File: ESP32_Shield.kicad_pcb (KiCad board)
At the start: 4 copper layers, 69 x 40.6 mm, 36 parts, among them J1 BME280, SHT40 Module, J10 SCD40 Module, J11 Conn_01x03, J12 Conn_01x03, J2 SCD40 Module, J3 Conn_01x02, J4 Qwiic_Vertical, J5 Conn_01x02, J6 Conn_01x02, J7 Conn_01x03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

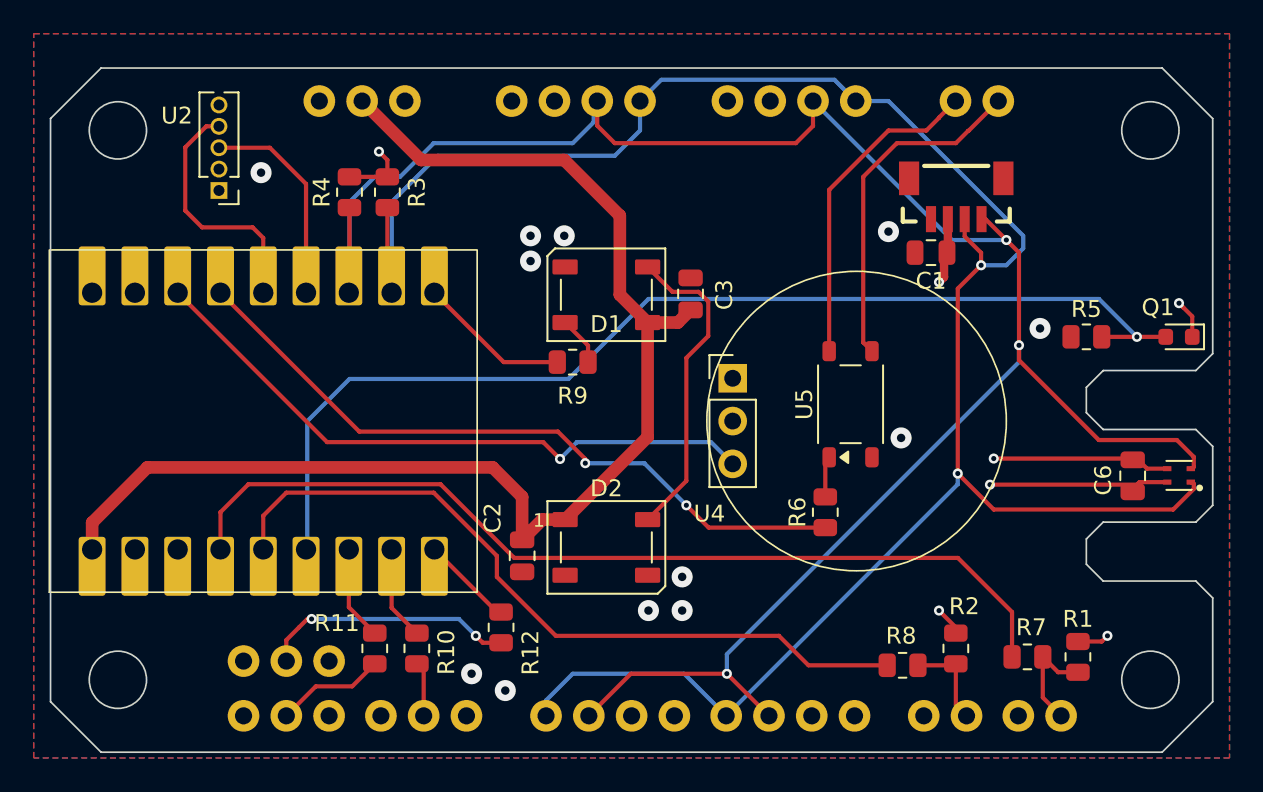
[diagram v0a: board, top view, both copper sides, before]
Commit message: remove fix soldered tempertaure sesor
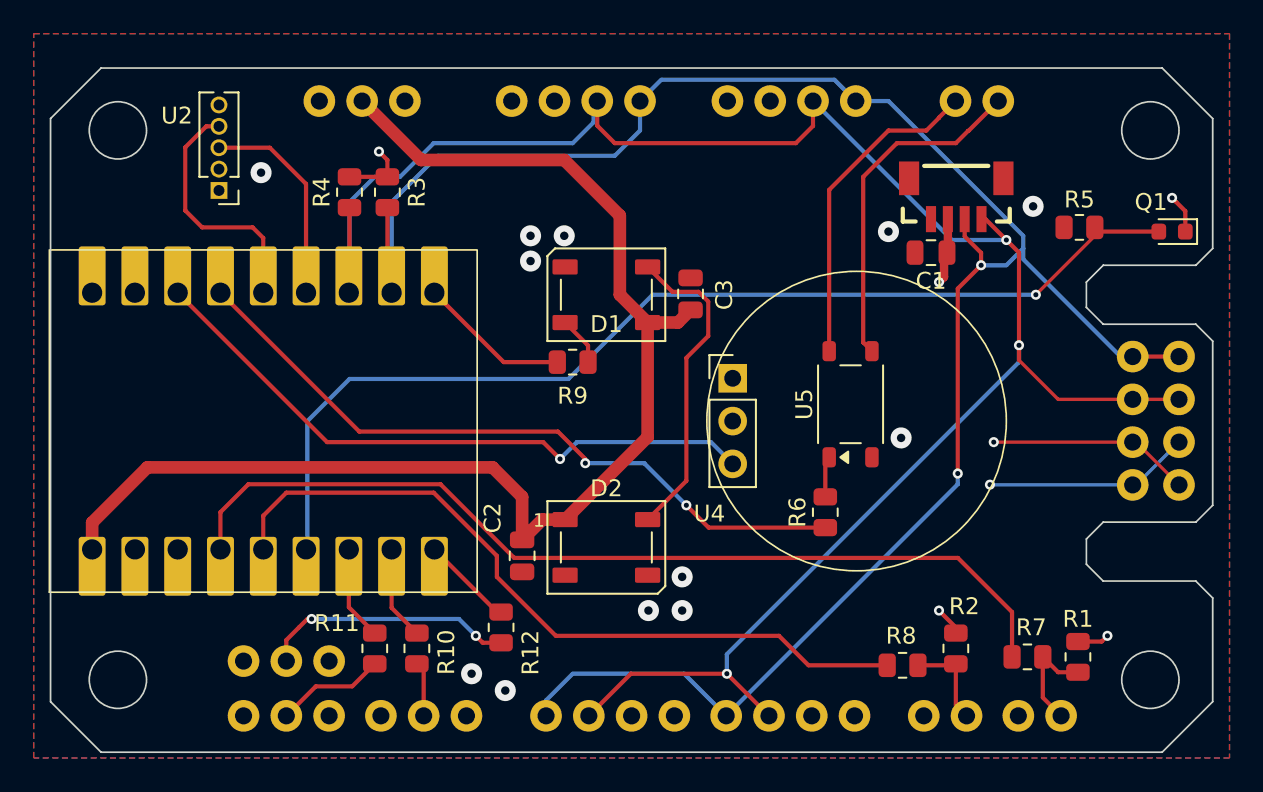
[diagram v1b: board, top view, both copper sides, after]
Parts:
- removed C6: 100n, Capacitor_SMD:C_0805_2012Metric
- removed U3: SHT40, PCM_SparkFun-Sensor:Sensirion_DFN-4_1.5x1.5mm_P0.8mm_SHT4x_NoCentralPad
- added J13: SCD40 Module, PCM_SparkFun-Connector:1x04_P2.54mm, F.Cu at (155.2, 92.3)
- added J14: BME280, SHT40 Module, PCM_SparkFun-Connector:1x04_P2.54mm, F.Cu at (158.0, 92.3)
- moved R5 6.51 mm to (152.1, 77.0)
- moved Q1 6.26 mm to (157.6, 77.2)
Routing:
- net SDA: track 125.1 -> 121.3 mm
- net SCK: track 122.4 -> 119.2 mm
- net GND: track 10.6 -> 12.3 mm
- net +3V3: track 24.4 -> 25.9 mm
- net PhotoMeas: track 64.6 -> 63.3 mm
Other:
- outline, holes or cut-outs redrawn

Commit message: add silk screen and mmWave connector
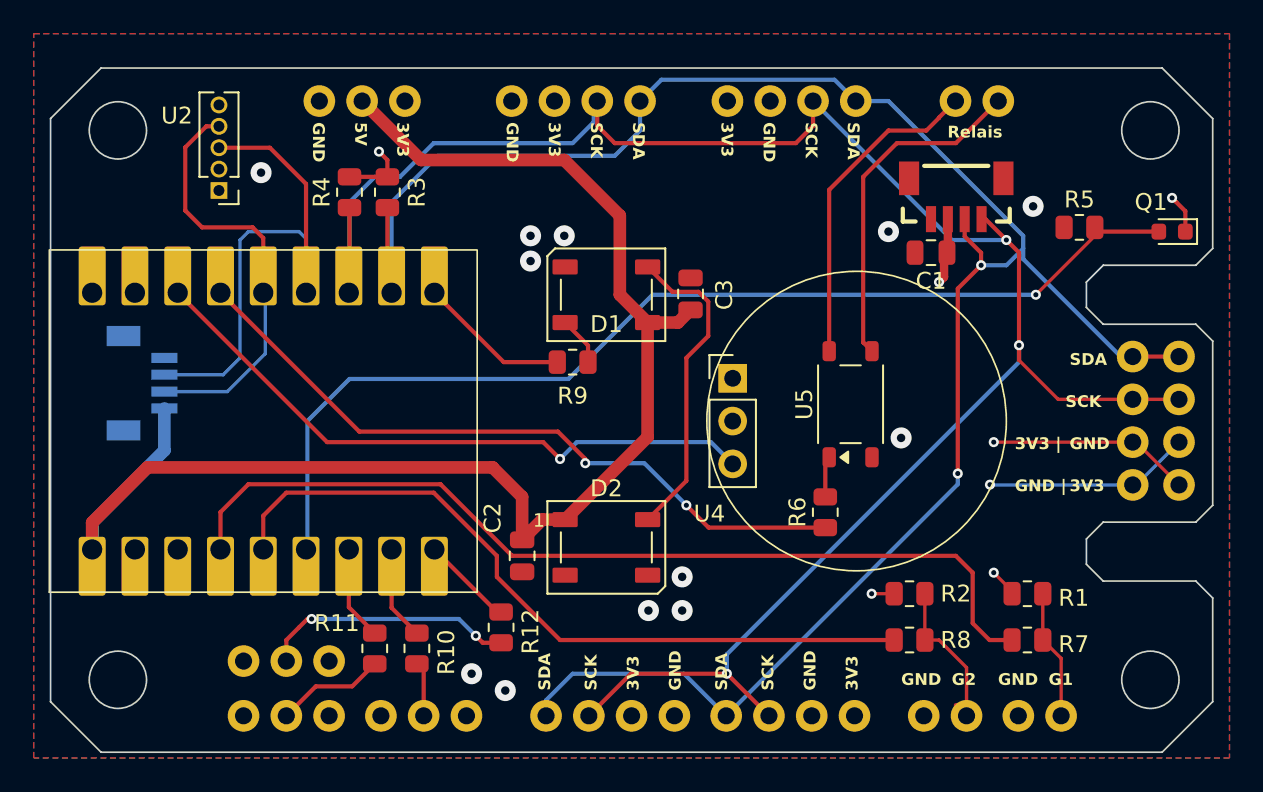
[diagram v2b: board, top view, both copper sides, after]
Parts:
- added J15: mmWave Connector, PCM_SparkFun-Connector:JST_1x04_P1.0mm_Vertical_SMD, B.Cu at (96.2, 86.2)
- moved R1 4.80 mm to (149.0, 98.8), turned to 180 degrees
- moved R2 4.26 mm to (142.0, 98.8), turned to 180 degrees
- moved R8 1.56 mm to (142.0, 101.5)
- moved R7 1.00 mm to (149.0, 101.5)
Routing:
- net UART_RX_mmWAVE: track 12.5 -> 31.9 mm
- net UART_TX_mmWAVE: track 14.8 -> 25.4 mm
- net +5V: track 76.5 -> 86.7 mm
- net Net-(J5-Pin_2): track 5.64 -> 9.66 mm
- net Net-(J6-Pin_2): track 6.42 -> 7.70 mm
- net +3V3: track 25.9 -> 25.3 mm
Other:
- board text added: "3V3"
- board text added: "3V3 |"
- board text added: "5V"
- board text added: "G1"
- board text added: "G2"
- board text added: "GND"
- board text added: "GND |"
- board text added: "Relais"
- board text added: "SCK"
- board text added: "SDA"

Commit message: add more JST connectors for UART
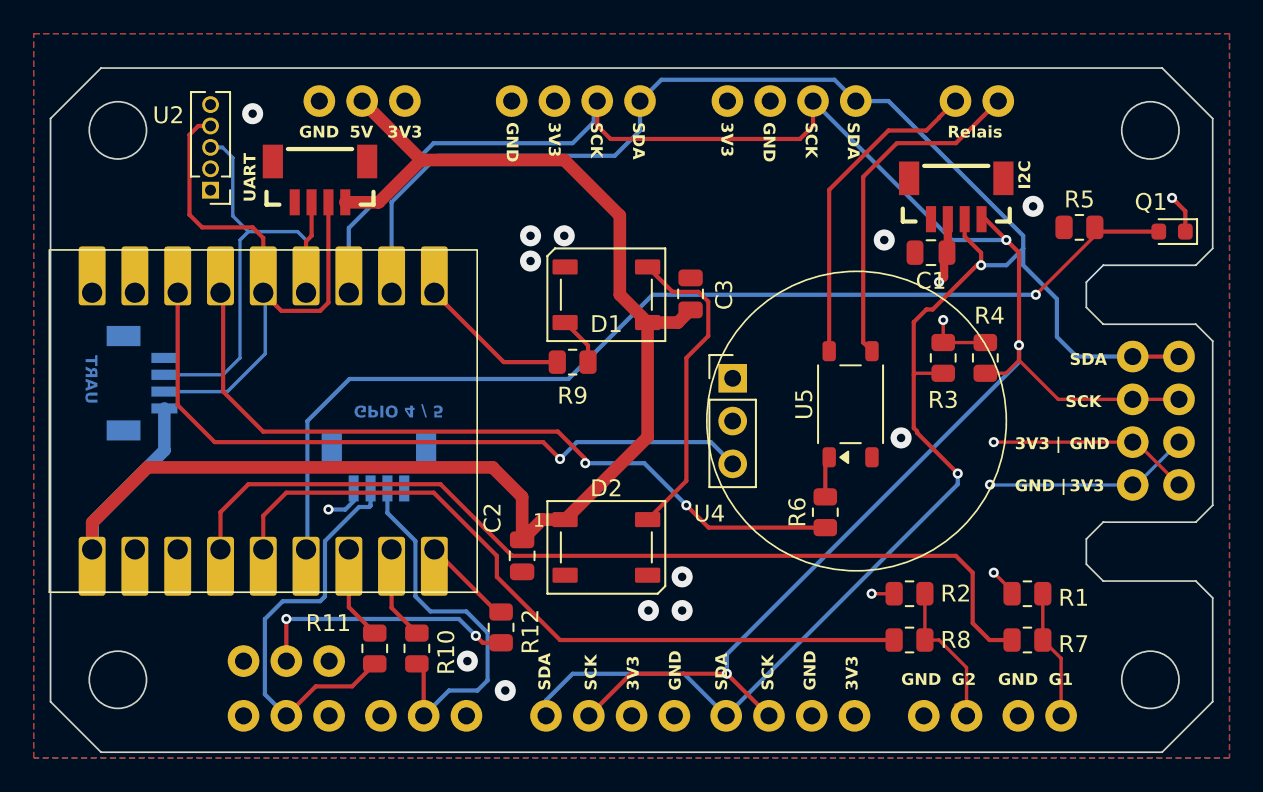
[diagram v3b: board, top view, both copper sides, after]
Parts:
- added J16: mmWave Connector, PCM_SparkFun-Connector:JST_1x04_P1.0mm_Vertical_SMD, F.Cu at (107.0, 74.0)
- added J17: mmWave Connector, PCM_SparkFun-Connector:JST_1x04_P1.0mm_Vertical_SMD, B.Cu at (110.5, 91.0)
- moved R4 39.0 mm to (146.5, 84.8)
- moved R3 34.4 mm to (144.0, 84.8)
- moved U2 0.50 mm to (100.5, 72.2)
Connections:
- net Net-(J7-Pin_2) renamed GPIO_4_
- net Net-(J8-Pin_2) renamed GPIO_5_
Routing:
- net GPIO_5_: track 3.26 -> 23.0 mm
- net GPIO_4_: track 6.53 -> 24.8 mm
- net UART_TX_mmWAVE: track 25.4 -> 35.5 mm
- net +5V: track 86.7 -> 92.5 mm
- net PIR: track 38.0 -> 41.9 mm
- net SCK: track 119.2 -> 115.5 mm
- net Relais: track 41.8 -> 45.2 mm
- net +3V3: track 25.3 -> 27.7 mm, vias 6 -> 7
- net SDA: track 121.3 -> 122.4 mm
- net Net-(J12-Pin_2): track 15.1 -> 15.8 mm
- net UART_RX_mmWAVE: track 31.9 -> 31.2 mm
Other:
- board text added: "GPIO 4 / 5"
- board text added: "I2C"
- board text added: "UART"

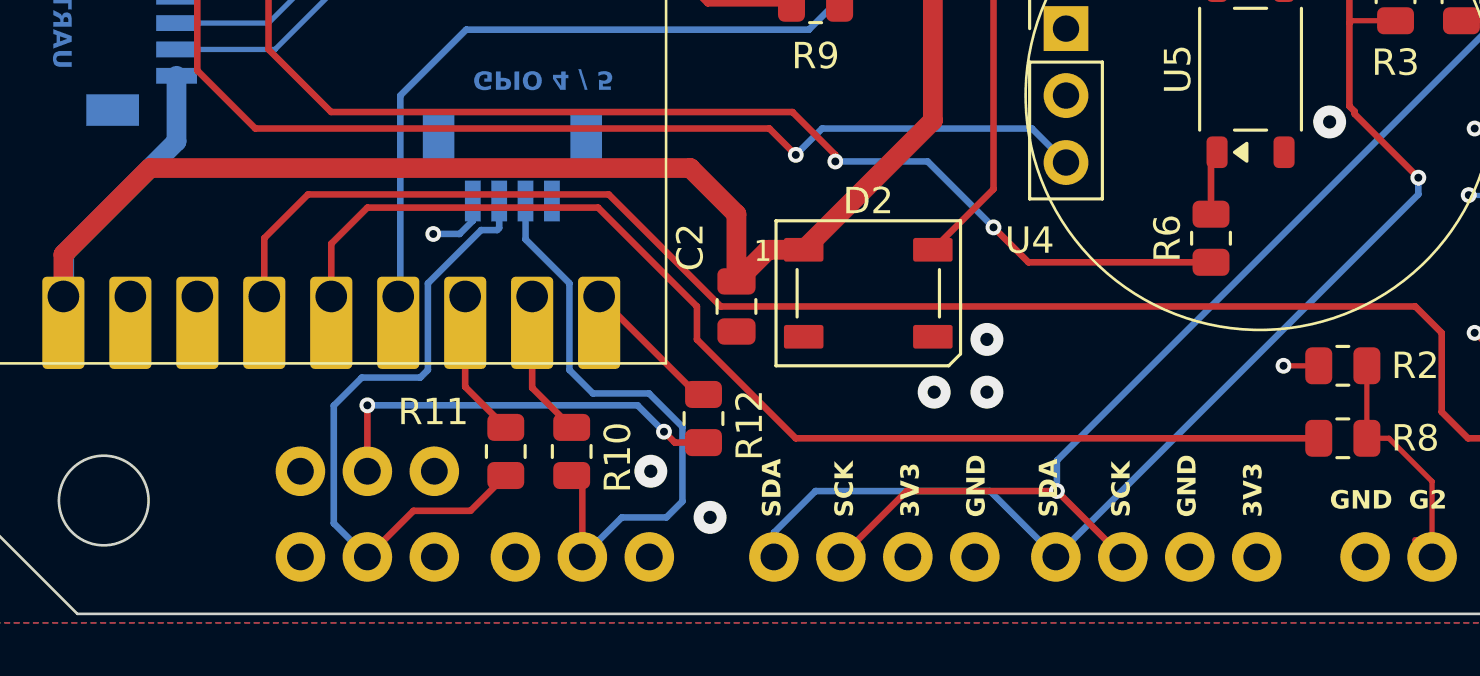
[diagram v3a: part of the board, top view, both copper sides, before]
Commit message: add jst connector for aditional gpios
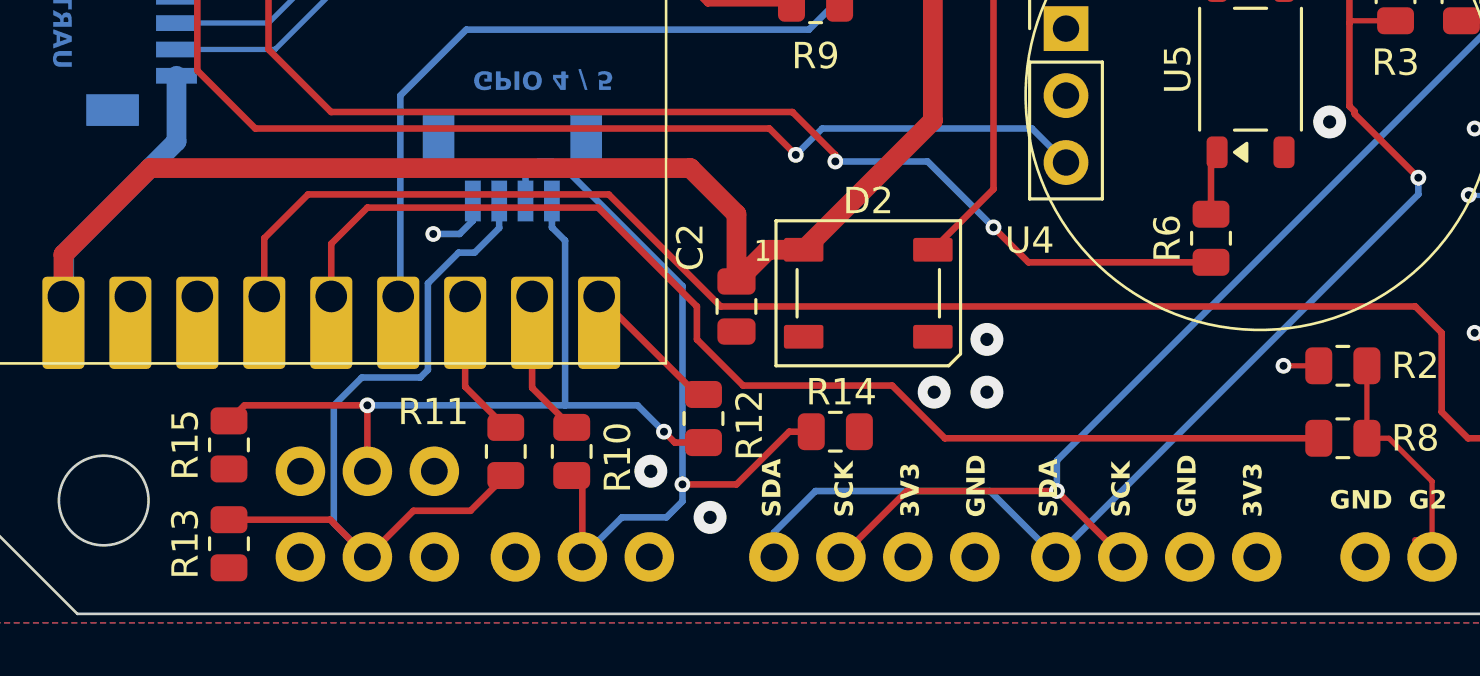
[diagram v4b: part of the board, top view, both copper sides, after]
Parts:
- added R13: 2k2, Resistor_SMD:R_0805_2012Metric, F.Cu at (99.8, 105.5)
- added R14: 2k2, Resistor_SMD:R_0805_2012Metric, F.Cu at (122.8, 101.2)
- added R15: 2k2, Resistor_SMD:R_0805_2012Metric, F.Cu at (99.8, 101.8)
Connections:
- J12 pad 2: Net-(J12-Pin_2) -> GPIO_6_
- J17 pad 1: GND -> GPIO_6_
- R12 pad 1: Net-(J12-Pin_2) -> GPIO_6_
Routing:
- net GPIO_6_: track 0.00 -> 29.3 mm, vias 0 -> 2
- net Net-(J12-Pin_2): track 15.8 -> 0.00 mm, vias 2 -> 0
- net GPIO_5_: track 23.0 -> 30.9 mm, vias 0 -> 1
- net GPIO_4_: track 24.8 -> 30.6 mm
